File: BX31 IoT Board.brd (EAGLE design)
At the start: 45 x 22.3 mm, 17 parts, among them IC1 CAT24C32 YI-GT3, Q1 BSS138, Q2 BSS138, Q3 BSS138

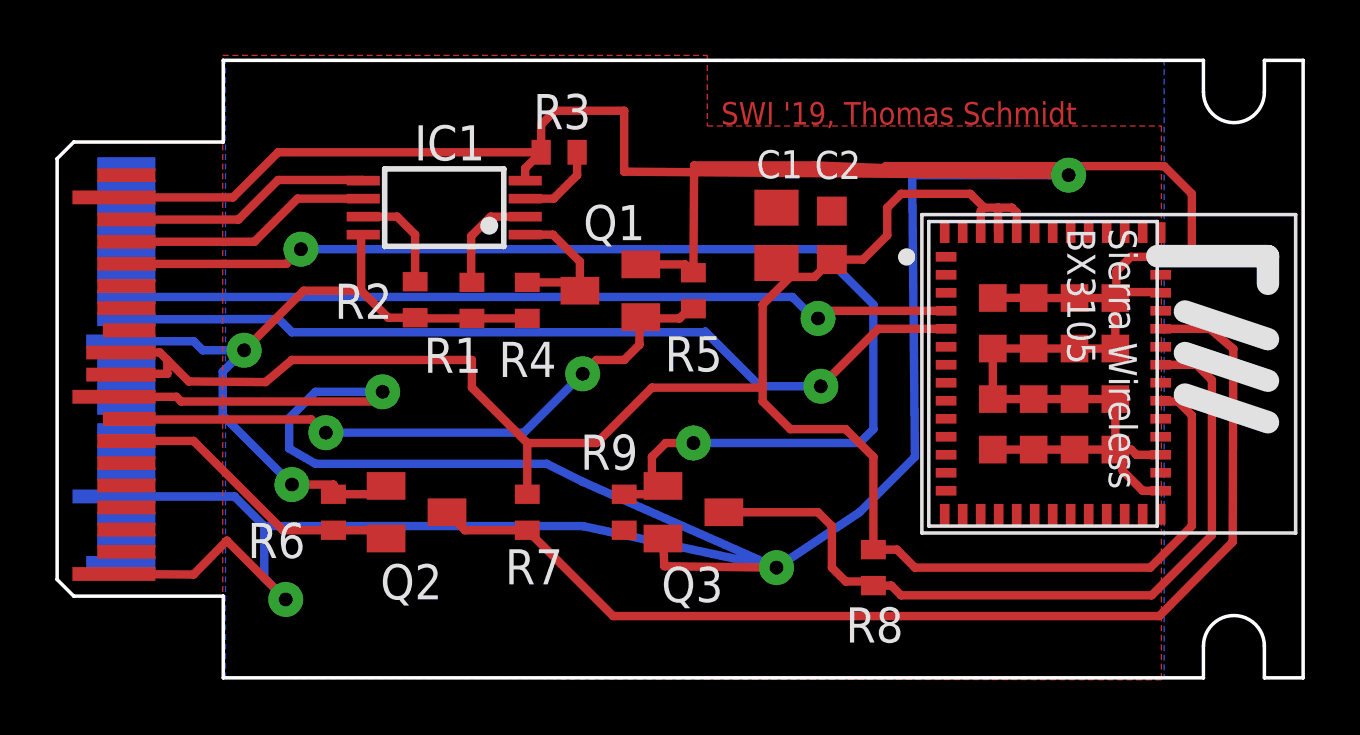
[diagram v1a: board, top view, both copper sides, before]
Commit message: removed BX31 Pin 33 supply, added testpoint for EEPROM, fixerd layout
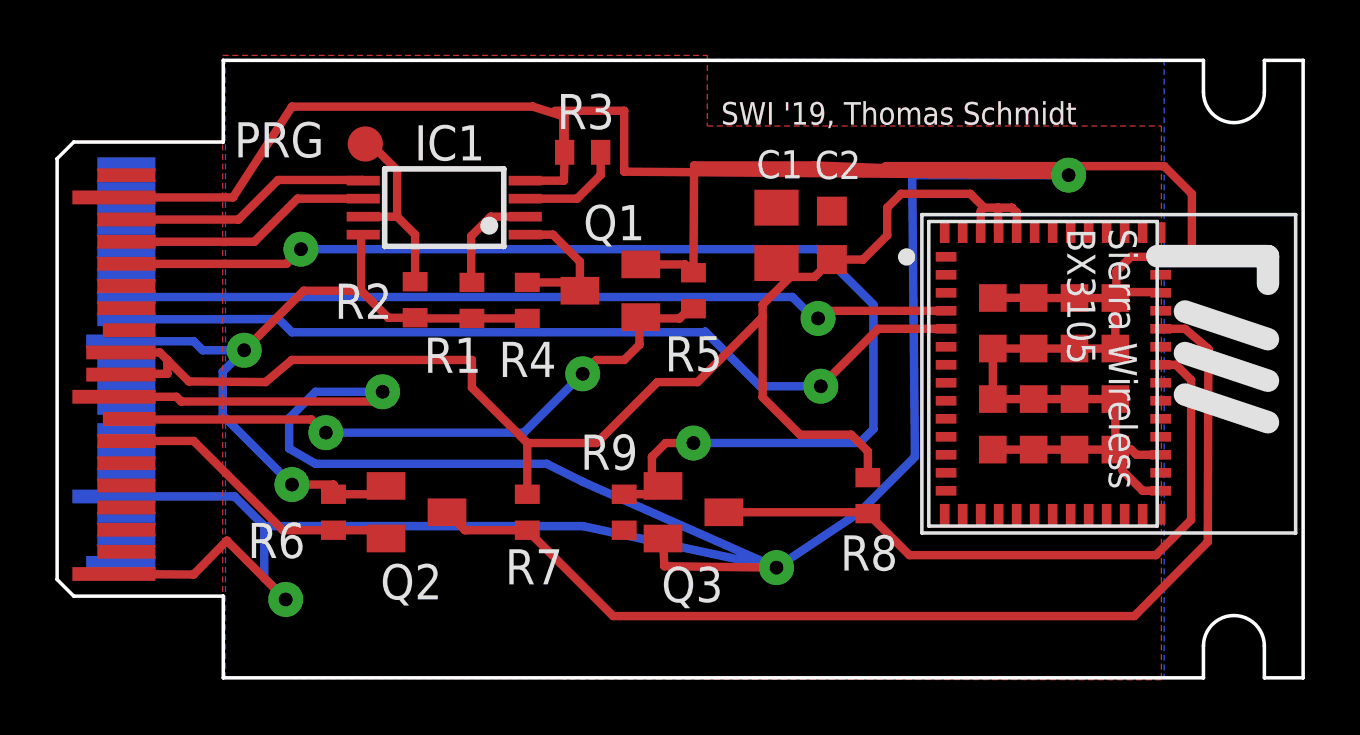
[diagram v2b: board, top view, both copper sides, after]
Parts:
- added PRG: TPSB1,27, testpad:B1,27
- moved R8 2.61 mm to (29.3, 6.60)
- moved R3 0.85 mm to (19.0, 19.0)
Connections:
- new net VDD_SDIO: MODULE1.33
- net EEPROM_WP: now also PRG.TP
- net VCC_3V3: no longer MODULE1.33
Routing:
- net VCC_3V3: track 75.0 -> 55.6 mm
- net GND: track 208.3 -> 212.5 mm
- net FW_UPDATE: track 28.3 -> 24.4 mm
- net EEPROM_WP: track 3.84 -> 7.06 mm
- net ENABLE: track 40.9 -> 39.1 mm
- net EEPROM_A2: track 3.05 -> 3.90 mm
